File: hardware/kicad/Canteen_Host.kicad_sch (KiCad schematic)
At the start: 12 parts, among them J2 ST7789 2.8in 320x240, J3 DS3231 ZS-042, J4 Battery 1S Li-ion, J5 microSD on LCD module, SW1 Tactile switch, U1 ESP32-S3-DevKitC-1 N16R8

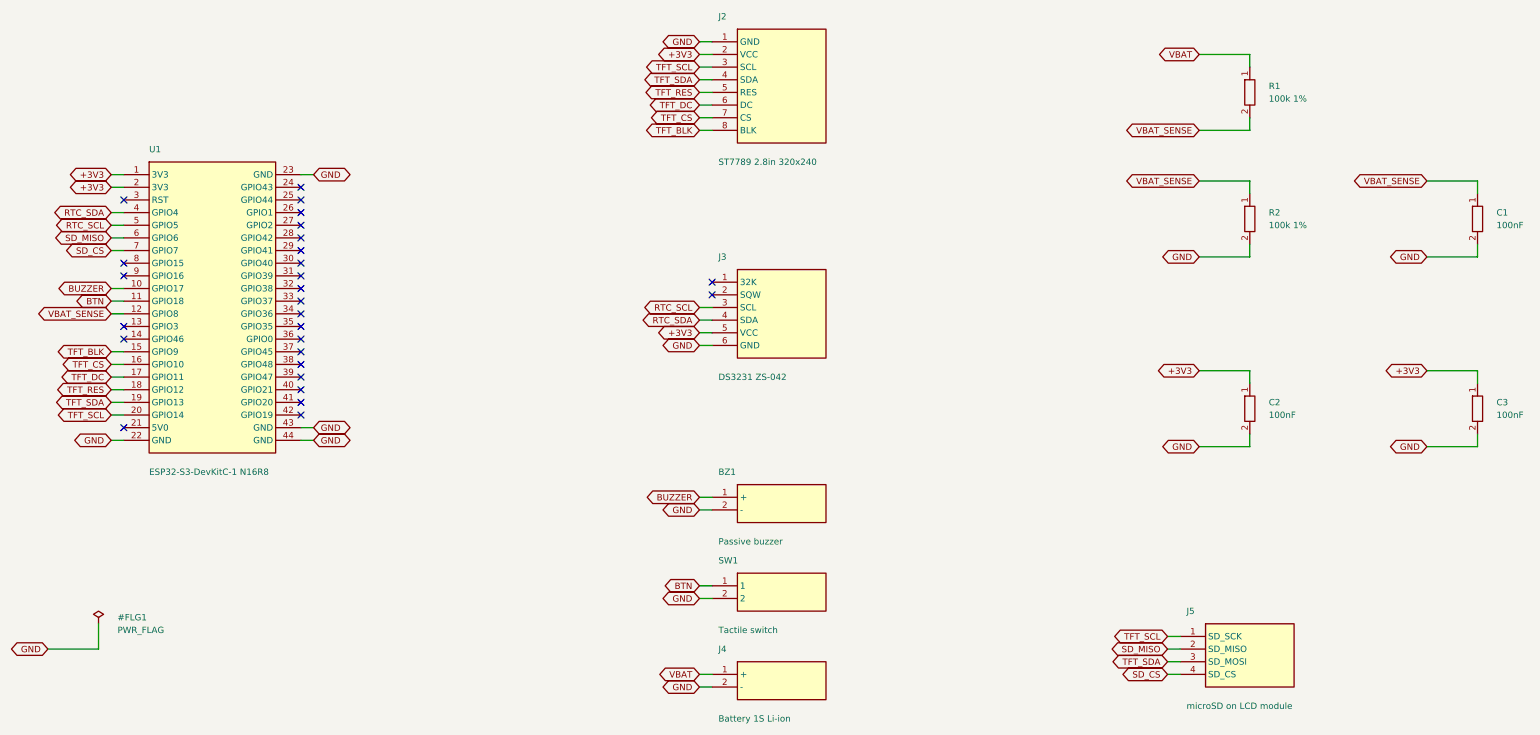
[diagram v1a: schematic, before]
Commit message: ย้ายการ์ด SD ไปอยู่บัส SPI ของตัวเอง ไม่ใช้ร่วมกับจอ (Host 113.12.0)
การแชร์บัสใช้งานได้จริงและเป็นวิธีมาตรฐาน ฝั่งซอฟต์แวร์ปลอดภัยเพราะไลบรารี SD
ใน arduino-esp32 เรียก beginTransaction และ endTransaction ทุกครั้งเหมือน Adafruit
และความเสี่ยงเรื่องการ์ดไม่ปล่อยขา MISO ก็ใช้ไม่ได้กับผังนี้เพราะจอไม่มีสาย MISO

แต่เลือกแยกด้วยสามเหตุผล หนึ่ง การแชร์บัสต้องเอาสายสองเส้นยัดเข้าหัวต่อเดียวกัน
ที่ GPIO13 กับ GPIO14 ซึ่งเป็นจุดที่หลุดง่ายที่สุดในงานที่ไขสายด้วยมือ
ส่วนแบบแยกคือสี่สายไปสี่ขาที่เรียงติดกัน หนึ่งต่อหนึ่ง ตามลำดับขาบนตัวโมดูล
สอง สายหลุดเส้นเดียวไม่ทำให้จอกับการ์ดดับพร้อมกัน
สาม ไลบรารี ST77xx ตั้งความเร็วจอไว้ที่ 32 MHz การแตกแขนงสายเพิ่มที่ความถี่นั้น
ทำให้คุณภาพสัญญาณแย่ลง ที่ทำได้เพราะแม่ข่ายใช้ SPI ตัวเดียวคือ FSPI ส่วน HSPI ว่างสนิท

ขาใหม่ SD_SCK 6, SD_MISO 7, SD_MOSI 15, SD_CS 16 อยู่ตำแหน่ง 6 ถึง 9 เรียงติดกัน
เพิ่ม SPIClass SPI_SD(HSPI) และคืนบัสของจอกลับเป็นไม่มี MISO เหมือนเดิม
เพราะจอไม่เคยต้องอ่านข้อมูลกลับ รุ่นที่แล้วต้องใส่เพราะการ์ดใช้บัสร่วมกัน
ตรวจซอร์สแล้วว่า SPIClass::begin คืนค่าทันทีถ้าบัสเปิดอยู่ การเรียกซ้ำตอนลองเมานต์ใหม่
ทุกสามสิบวินาทีจึงปลอดภัย

สร้างไฟล์วงจร KiCad ใหม่ การ์ดมีเน็ตของตัวเองครบสี่เส้น
และคืนกติกาของ kicadcheck.py ให้เข้มเหมือนเดิม รุ่นที่แล้วต้องผ่อนให้ TFT_SCL
กับ TFT_SDA มีสามปลายได้เพราะใช้บัสร่วมกัน ตอนนี้ตั้งรายการนั้นเป็นค่าว่าง
กลับไปบังคับว่าเน็ตสัญญาณทุกเส้นต้องมีสองปลายพอดี ตัวตรวจทั้งสิบตัวผ่าน

Co-Authored-By: Claude Opus 5 <noreply@anthropic.com>
Claude-Session: https://claude.ai/code/session_01X9SBq9sFrEp9tTPMPW8bbn
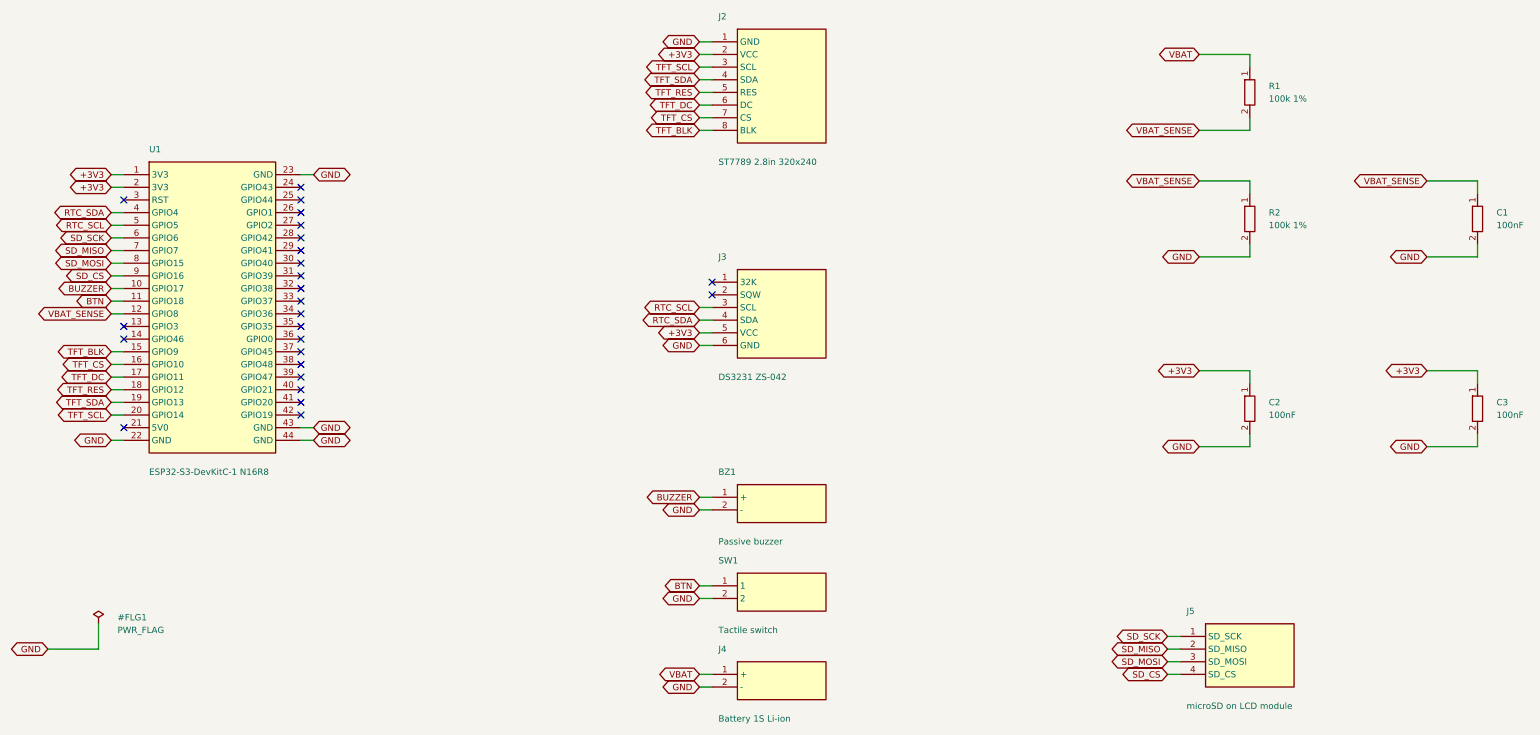
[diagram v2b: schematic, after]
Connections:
- net SD_CS: now also U1.9 (GPIO16); no longer U1.7 (GPIO7)
- net SD_MISO: now also U1.7 (GPIO7); no longer U1.6 (GPIO6)
- net TFT_SCL: no longer J5.1 (SD_SCK)
- net TFT_SDA: no longer J5.3 (SD_MOSI)
- net SD_MOSI: now reaches U1.8 (GPIO15)
- net SD_MOSI: now also J5.3 (SD_MOSI)
- new net SD_SCK: J5.1 (SD_SCK), U1.6 (GPIO6)
- no-connect marks 27 -> 25
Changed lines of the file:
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@@
     (pin "43")
     (pin "44")
-    (instances (project "Canteen_Host" (path "/d3199036-6fd6-40f2-83a0-9a5671a86bb7" (reference "U1") (unit 1))))
+    (instances (project "Canteen_Host" (path "/e2ba2733-9a18-4733-97a8-587326f851be" (reference "U1") (unit 1))))
   )
   (wire (pts (xy 58.42 82.55) (xy 55.88 82.55))
@@
     (stroke (width 0) (type default))
   )
-  (global_label "SD_MISO" (shape bidirectional) (at 55.88 95.25 180) (fields_autoplaced)
+  (global_label "SD_SCK" (shape bidirectional) (at 55.88 95.25 180) (fields_autoplaced)
     (effects (font (size 1.27 1.27)) (justify right))
     (property "Intersheetrefs" "${INTERSHEET_REFS}" (at 0 0 0)
@@
     (stroke (width 0) (type default))
   )
-  (global_label "SD_CS" (shape bidirectional) (at 55.88 97.79 180) (fields_autoplaced)
-    (effects (font (size 1.27 1.27)) (justify right))
-    (property "Intersheetrefs" "${INTERSHEET_REFS}" (at 0 0 0)
-      (effects (font (size 1.27 1.27)) hide))
-  )
-  (no_connect (at 58.42 100.33))
-  (no_connect (at 58.42 102.87))
+  (global_label "SD_MISO" (shape bidirectional) (at 55.88 97.79 180) (fields_autoplaced)
+    (effects (font (size 1.27 1.27)) (justify right))
+    (property "Intersheetrefs" "${INTERSHEET_REFS}" (at 0 0 0)
+      (effects (font (size 1.27 1.27)) hide))
+  )
+  (wire (pts (xy 58.42 100.33) (xy 55.88 100.33))
+    (stroke (width 0) (type default))
+  )
+  (global_label "SD_MOSI" (shape bidirectional) (at 55.88 100.33 180) (fields_autoplaced)
+    (effects (font (size 1.27 1.27)) (justify right))
+    (property "Intersheetrefs" "${INTERSHEET_REFS}" (at 0 0 0)
+      (effects (font (size 1.27 1.27)) hide))
+  )
+  (wire (pts (xy 58.42 102.87) (xy 55.88 102.87))
+    (stroke (width 0) (type default))
+  )
+  (global_label "SD_CS" (shape bidirectional) (at 55.88 102.87 180) (fields_autoplaced)
+    (effects (font (size 1.27 1.27)) (justify right))
+    (property "Intersheetrefs" "${INTERSHEET_REFS}" (at 0 0 0)
+      (effects (font (size 1.27 1.27)) hide))
+  )
   (wire (pts (xy 58.42 105.41) (xy 55.88 105.41))
     (stroke (width 0) (type default))
@@
     (pin "7")
     (pin "8")
-    (instances (project "Canteen_Host" (path "/d3199036-6fd6-40f2-83a0-9a5671a86bb7" (reference "J2") (unit 1))))
+    (instances (project "Canteen_Host" (path "/e2ba2733-9a18-4733-97a8-587326f851be" (reference "J2") (unit 1))))
   )
   (wire (pts (xy 176.53 55.88) (xy 173.99 55.88))
@@
     (pin "5")
     (pin "6")
-    (instances (project "Canteen_Host" (path "/d3199036-6fd6-40f2-83a0-9a5671a86bb7" (reference "J3") (unit 1))))
+    (instances (project "Canteen_Host" (path "/e2ba2733-9a18-4733-97a8-587326f851be" (reference "J3") (unit 1))))
   )
   (no_connect (at 176.53 104.14))
@@
     (pin "3")
     (pin "4")
-    (instances (project "Canteen_Host" (path "/d3199036-6fd6-40f2-83a0-9a5671a86bb7" (reference "J5") (unit 1))))
+    (instances (project "Canteen_Host" (path "/e2ba2733-9a18-4733-97a8-587326f851be" (reference "J5") (unit 1))))
   )
   (wire (pts (xy 270.51 175.26) (xy 267.97 175.26))
     (stroke (width 0) (type default))
   )
-  (global_label "TFT_SCL" (shape bidirectional) (at 267.97 175.26 180) (fields_autoplaced)
+  (global_label "SD_SCK" (shape bidirectional) (at 267.97 175.26 180) (fields_autoplaced)
     (effects (font (size 1.27 1.27)) (justify right))
     (property "Intersheetrefs" "${INTERSHEET_REFS}" (at 0 0 0)
@@
     (stroke (width 0) (type default))
   )
-  (global_label "TFT_SDA" (shape bidirectional) (at 267.97 180.34 180) (fields_autoplaced)
+  (global_label "SD_MOSI" (shape bidirectional) (at 267.97 180.34 180) (fields_autoplaced)
     (effects (font (size 1.27 1.27)) (justify right))
     (property "Intersheetrefs" "${INTERSHEET_REFS}" (at 0 0 0)
@@
     (pin "1")
     (pin "2")
-    (instances (project "Canteen_Host" (path "/d3199036-6fd6-40f2-83a0-9a5671a86bb7" (reference "BZ1") (unit 1))))
+    (instances (project "Canteen_Host" (path "/e2ba2733-9a18-4733-97a8-587326f851be" (reference "BZ1") (unit 1))))
   )
   (wire (pts (xy 176.53 147.32) (xy 173.99 147.32))
@@
     (pin "1")
     (pin "2")
-    (instances (project "Canteen_Host" (path "/d3199036-6fd6-40f2-83a0-9a5671a86bb7" (reference "SW1") (unit 1))))
+    (instances (project "Canteen_Host" (path "/e2ba2733-9a18-4733-97a8-587326f851be" (reference "SW1") (unit 1))))
   )
   (wire (pts (xy 176.53 165.10) (xy 173.99 165.10))
@@
     (pin "1")
     (pin "2")
-    (instances (project "Canteen_Host" (path "/d3199036-6fd6-40f2-83a0-9a5671a86bb7" (reference "J4") (unit 1))))
+    (instances (project "Canteen_Host" (path "/e2ba2733-9a18-4733-97a8-587326f851be" (reference "J4") (unit 1))))
   )
   (wire (pts (xy 176.53 182.88) (xy 173.99 182.88))
@@
     (pin "1")
     (pin "2")
-    (instances (project "Canteen_Host" (path "/d3199036-6fd6-40f2-83a0-9a5671a86bb7" (reference "R1") (unit 1))))
+    (instances (project "Canteen_Host" (path "/e2ba2733-9a18-4733-97a8-587326f851be" (reference "R1") (unit 1))))
   )
   (wire (pts (xy 284.48 60.96) (xy 284.48 58.42))
@@
     (pin "1")
     (pin "2")
-    (instances (project "Canteen_Host" (path "/d3199036-6fd6-40f2-83a0-9a5671a86bb7" (reference "R2") (unit 1))))
+    (instances (project "Canteen_Host" (path "/e2ba2733-9a18-4733-97a8-587326f851be" (reference "R2") (unit 1))))
   )
   (wire (pts (xy 284.48 86.36) (xy 284.48 83.82))
@@
     (pin "1")
     (pin "2")
-    (instances (project "Canteen_Host" (path "/d3199036-6fd6-40f2-83a0-9a5671a86bb7" (reference "C1") (unit 1))))
+    (instances (project "Canteen_Host" (path "/e2ba2733-9a18-4733-97a8-587326f851be" (reference "C1") (unit 1))))
   )
   (wire (pts (xy 330.20 86.36) (xy 330.20 83.82))
@@
     (pin "1")
     (pin "2")
-    (instances (project "Canteen_Host" (path "/d3199036-6fd6-40f2-83a0-9a5671a86bb7" (reference "C2") (unit 1))))
+    (instances (project "Canteen_Host" (path "/e2ba2733-9a18-4733-97a8-587326f851be" (reference "C2") (unit 1))))
   )
   (wire (pts (xy 284.48 124.46) (xy 284.48 121.92))
@@
     (pin "1")
     (pin "2")
-    (instances (project "Canteen_Host" (path "/d3199036-6fd6-40f2-83a0-9a5671a86bb7" (reference "C3") (unit 1))))
+    (instances (project "Canteen_Host" (path "/e2ba2733-9a18-4733-97a8-587326f851be" (reference "C3") (unit 1))))
   )
   (wire (pts (xy 330.20 124.46) (xy 330.20 121.92))
@@
     (property "Datasheet" "" (at 0 0 0) (effects (font (size 1.27 1.27)) hide))
     (pin "1")
-    (instances (project "Canteen_Host" (path "/d3199036-6fd6-40f2-83a0-9a5671a86bb7" (reference "#FLG1") (unit 1))))
+    (instances (project "Canteen_Host" (path "/e2ba2733-9a18-4733-97a8-587326f851be" (reference "#FLG1") (unit 1))))
   )
   (wire (pts (xy 53.34 172.72) (xy 53.34 177.80))
